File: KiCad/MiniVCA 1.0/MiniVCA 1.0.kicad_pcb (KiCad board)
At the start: 2 copper layers, 62 x 128.5 mm, 31 parts, among them J1 CV_2, J2 CV_1, J3 AudioIn, J4 AudioOut, J5 JST_BUS, J6 IDC_BUS, Q1 BC559, U1 LM13700, U2 TL072

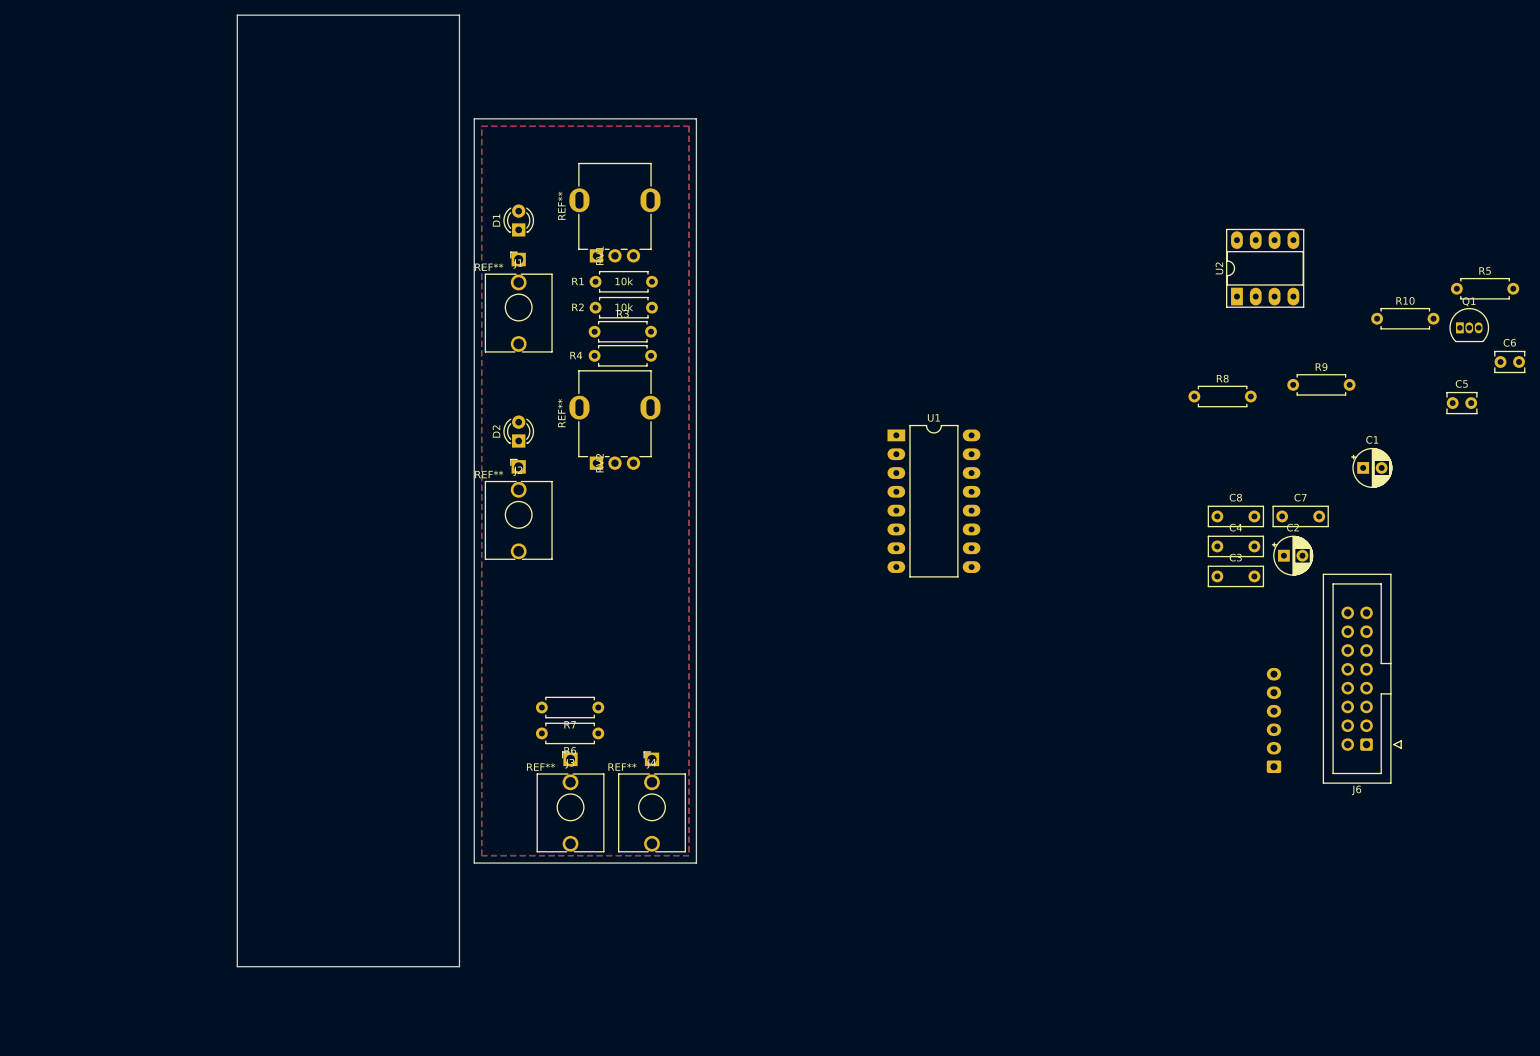
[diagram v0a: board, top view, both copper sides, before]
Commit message: Added 4hp pcb
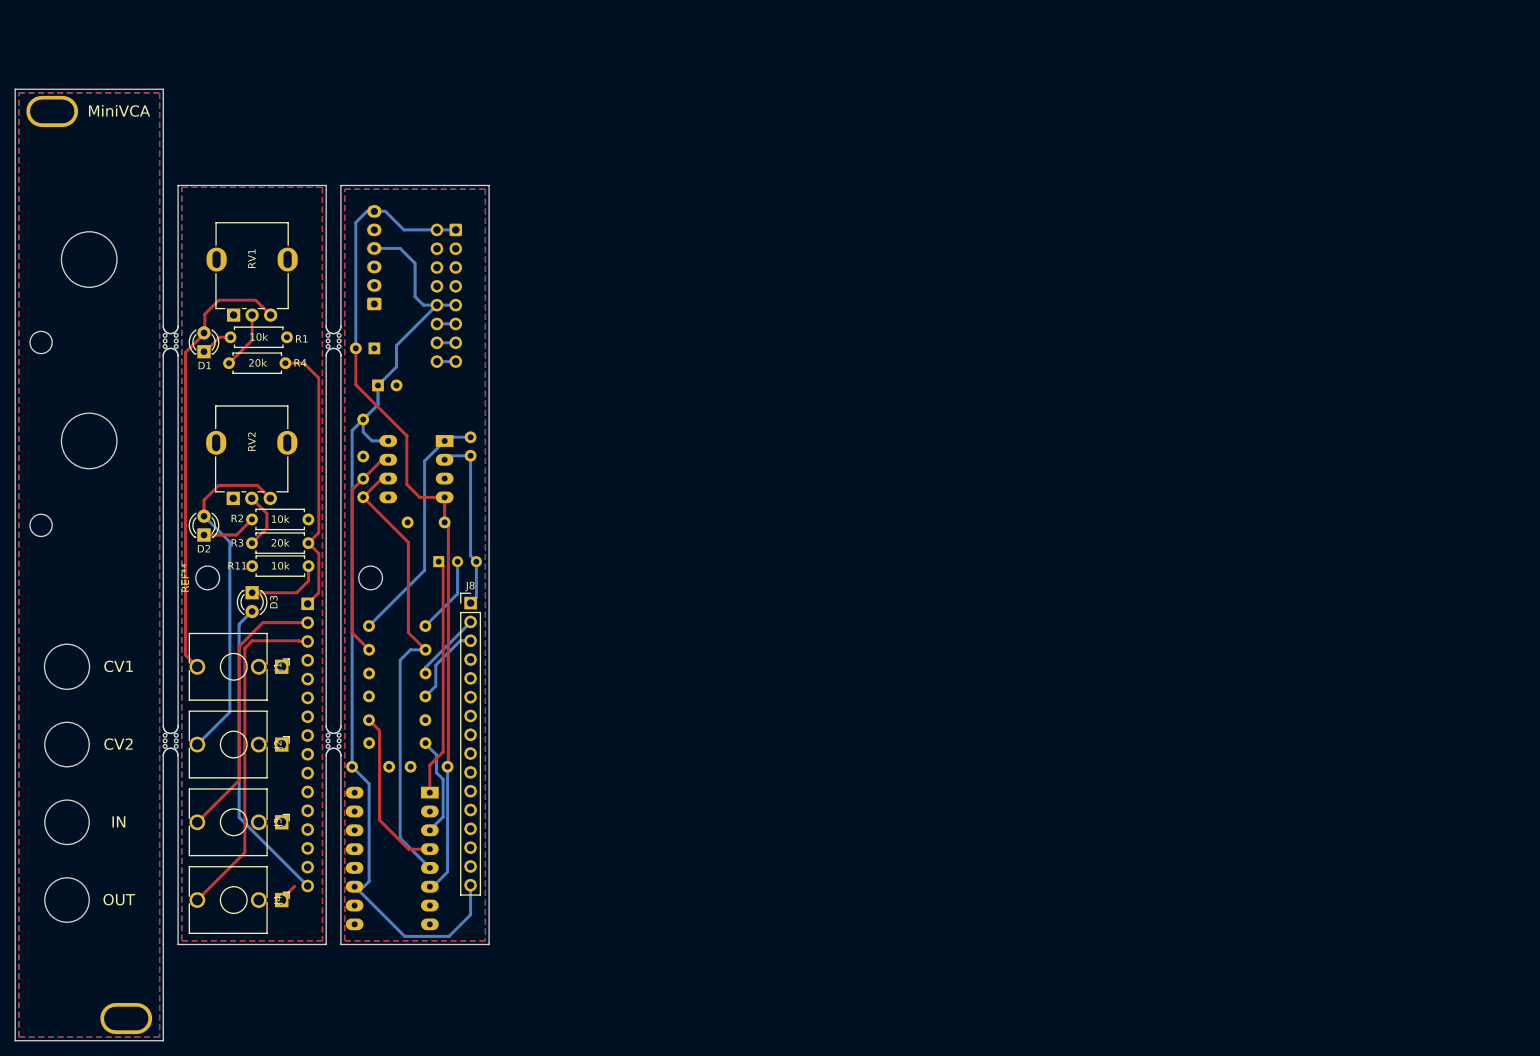
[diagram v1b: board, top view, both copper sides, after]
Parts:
- added D3: LED, LED_THT:LED_D3.0mm, F.Cu at (82.0, 108.0)
- added J7: BOARD1_HEADERS, Connector_PinSocket_2.54mm:PinSocket_1x16_P2.54mm_Vertical, B.Cu at (89.5, 109.5)
- added J8: BOARD2_HEADERS, Connector_PinHeader_2.54mm:PinHeader_1x16_P2.54mm_Vertical, F.Cu at (111.5, 109.4)
- added R11: 10k, Resistor_THT:R_Axial_DIN0207_L6.3mm_D2.5mm_P7.62mm_Horizontal, F.Cu at (82.0, 104.4)
- added REF**: Panel_4HP, benjiaomodular:Panel_4HP, F.Cu at (50.0, 40.0)
- added REF**: MouseBite_2mm, benjiaomodular:MouseBite_2mm, F.Cu at (93.0, 128.0)
- added REF**: MouseBite_2mm, benjiaomodular:MouseBite_2mm, F.Cu at (93.0, 74.0)
- added REF**: MountingHole_3.2mm_M3, MountingHole:MountingHole_3.2mm_M3, F.Cu at (98.0, 106.0)
- added REF**: MountingHole_3.2mm_M3, MountingHole:MountingHole_3.2mm_M3, F.Cu at (76.0, 106.0)
- added REF**: MouseBite_2mm, benjiaomodular:MouseBite_2mm, F.Cu at (71.0, 128.0)
- added REF**: MouseBite_2mm, benjiaomodular:MouseBite_2mm, F.Cu at (71.0, 74.0)
- C1, C2, C3, C4, C5, C6, C7, C8, J6, R10, R5, R6, R7, R8, R9, U1, U2: moved to B.Cu
- Q1: footprint Package_TO_SOT_THT:TO-92_Inline -> Package_TO_SOT_THT:TO-92_Inline_Wide; moved to B.Cu
- moved R5 159.2 mm to (97.8, 128.3)
- moved C6 154.4 mm to (97.0, 92.6), turned to 270 degrees
- moved Q1 141.5 mm to (107.2, 103.8)
- moved J6 141.3 mm to (109.5, 59.0)
- moved R10 138.3 mm to (105.4, 122.0), turned to 180 degrees
- moved J5 136.6 mm to (98.5, 69.0)
- moved C1 133.5 mm to (99.0, 80.0)
- moved C5 132.7 mm to (111.5, 87.0), turned to 270 degrees
- moved R9 129.8 mm to (97.8, 115.7)
- moved C2 126.0 mm to (98.5, 75.0), turned to 180 degrees
- moved C7 124.4 mm to (97.0, 89.6), turned to 90 degrees
- moved C3 114.8 mm to (100.5, 131.5), turned to 180 degrees
- moved C4 112.9 mm to (103.4, 131.5)
- moved C8 109.4 mm to (103.0, 98.5)
- moved U2 108.8 mm to (108.0, 87.5), turned to 180 degrees
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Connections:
- net +12V renamed B2_12V
- C1 pad 2: GND -> GND2
- C2 pad 1: GND -> GND2
- C3 pad 1: GND -> GND2
- C4 pad 1: GND -> GND2
- C5 pad 2: Net-(C5-Pad2) -> B2_1
- C7 pad 1: GND -> GND2
- C8 pad 1: GND -> GND2
- J1 pad S: GND -> GND1
- J2 pad S: GND -> GND1
- J3 pad S: GND -> GND1
- J3 pad T: Net-(J3-PadT) -> B1_2
- J4 pad S: GND -> GND1
- J4 pad T: Net-(J4-PadT) -> B1_3
- J5 pad 5: GND -> GND2
- J6 pad 3: GND -> GND2
- J6 pad 4: GND -> GND2
- J6 pad 5: GND -> GND2
- J6 pad 6: GND -> GND2
- J6 pad 7: GND -> GND2
- J6 pad 8: GND -> GND2
- Q1 pad 3: Net-(C5-Pad2) -> B2_1
- R1 pad 1: GND -> GND1
- R10 pad 1: Net-(J4-PadT) -> B2_3
- R2 pad 1: GND -> GND1
- R3 pad 1: Net-(C5-Pad2) -> B1_1
- R4 pad 1: Net-(C5-Pad2) -> B1_1
- R5 pad 1: GND -> GND2
- R6 pad 2: Net-(J3-PadT) -> B2_2
- R7 pad 1: GND -> GND2
- RV1 pad 1: GND -> GND1
- RV2 pad 1: GND -> GND1
- U2 pad 2: Net-(C5-Pad2) -> B2_1
- U2 pad 3: GND -> GND2
- U2 pad 5: GND -> GND2
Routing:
- net B2_12V: track 0.00 -> 131.8 mm
- net -12V: track 0.00 -> 113.3 mm
- net Net-(C6-Pad2): track 0.00 -> 62.2 mm
- net Net-(D1-Pad2): track 0.00 -> 59.9 mm
- net Net-(D2-Pad2): track 0.00 -> 46.8 mm
- net B1_3: track 0.00 -> 45.6 mm
- net B1_12V: track 0.00 -> 41.7 mm
- net B1_1: track 0.00 -> 37.6 mm
- net B1_2: track 0.00 -> 36.7 mm
- net Net-(C5-Pad1): track 0.00 -> 32.9 mm
- net Net-(Q1-Pad1): track 0.00 -> 32.2 mm
- net Net-(C6-Pad1): track 0.00 -> 29.1 mm
- net B2_1: track 0.00 -> 24.3 mm
- net Net-(R6-Pad1): track 0.00 -> 22.5 mm
- net Net-(R5-Pad2): track 0.00 -> 13.5 mm
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- added copper zone on B.Cu, net (none)
- added copper zone on F.Cu, net (none)
- added copper zone on B.Cu, net GND1
- added copper zone on F.Cu, net GND1
- added copper zone on B.Cu, net GND2
- added copper zone on F.Cu, net GND2
- removed copper zone on B.Cu, net GND
- removed copper zone on F.Cu, net GND
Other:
- board size 62 x 128.5 mm -> 64 x 128.5 mm
- net class Default: trace_width 0.25 -> 0.4
- board text added: "@benjiaomodular"
- board text added: "CV1"
- board text added: "CV2"
- board text added: "IN"
- board text added: "MiniVCA"
- board text added: "OUT"
